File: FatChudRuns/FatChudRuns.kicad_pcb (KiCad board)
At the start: 4 copper layers, 96.9 x 73.9 mm, 104 parts, among them J1 RJ45_Pulse_JXD6-0001NL, J2 Z-21320110021001, J3 FTSH-107-01-L-DV-K-P, J4 TYPE-C-31-M-12, SW1 TS-1187A-B-A-B, SW5 1825360-3, U1 STM32F107RBT6, U2 DP83848I, U3 USBLC6-2SC6, U4 ST730M33R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

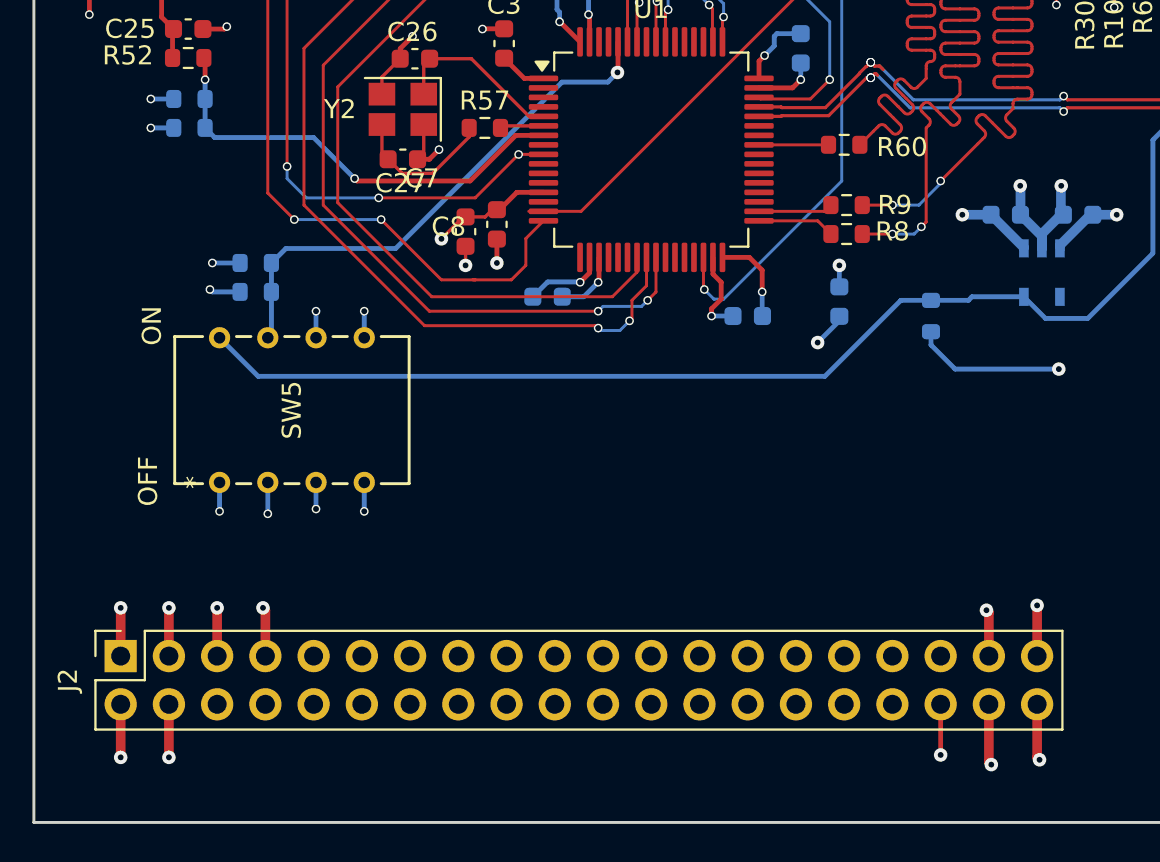
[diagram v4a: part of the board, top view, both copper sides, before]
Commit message: finished initial layout, removed some gpio pins and reorganized them
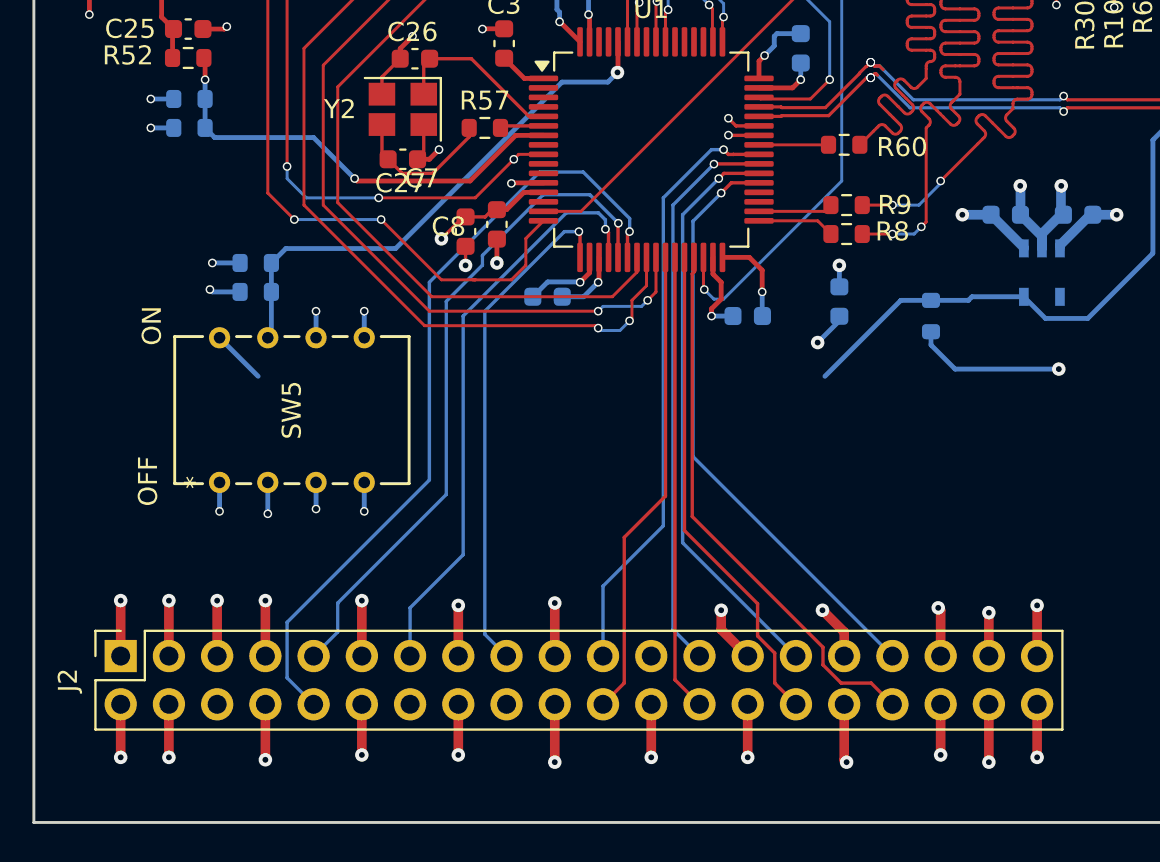
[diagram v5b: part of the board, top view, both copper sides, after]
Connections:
- J2 pad 10: /MCU/PA4 -> /MCU/PA6
- J2 pad 11: /MCU/PC0 -> GND
- J2 pad 12: /MCU/PA5 -> GND
- J2 pad 13: /MCU/PC2 -> /MCU/PA4
- J2 pad 14: /MCU/PA6 -> unconnected-(J2-Pin_14-Pad14)
- J2 pad 15: /MCU/PC3 -> GND
- J2 pad 16: /MCU/PA9 -> GND
- J2 pad 17: /MCU/PC6 -> /MCU/PA3
- J2 pad 18: /MCU/PA10 -> unconnected-(J2-Pin_18-Pad18)
- J2 pad 19: /MCU/PC7 -> GND
- J2 pad 20: /MCU/PB0 -> GND
- J2 pad 21: /MCU/PC8 -> /MCU/PC9
- J2 pad 22: /MCU/PB1 -> /MCU/PB0
- J2 pad 23: /MCU/PC9 -> GND
- J2 pad 24: /MCU/PB2 -> GND
- J2 pad 25: /MCU/PC10 -> /MCU/PC8
- J2 pad 26: /MCU/PB5 -> /MCU/PB1
- J2 pad 27: /MCU/PC11 -> GND
- J2 pad 28: /MCU/PB8 -> GND
- J2 pad 29: /MCU/PC12 -> /MCU/PC7
- J2 pad 30: /MCU/PB9 -> /MCU/PB2
- J2 pad 31: /MCU/PC13 -> GND
- J2 pad 32: /MCU/PB10 -> GND
- J2 pad 33: /MCU/PC14 -> /MCU/PC6
- J2 pad 34: /MCU/PB14 -> /MCU/PB10
- J2 pad 35: /MCU/PC15 -> GND
- J2 pad 36: /MCU/PB15 -> GND
- J2 pad 6: /MCU/PA0 -> +3.3V
- J2 pad 7: +3.3V -> GND
- J2 pad 8: /MCU/PA3 -> GND
- J2 pad 9: /MCU/PD2 -> /MCU/PA5
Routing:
- net GND: track 144.6 -> 188.2 mm, vias 71 -> 87
- net /MCU/PA6: track 0.00 -> 42.0 mm, vias 0 -> 1
- net /MCU/PA5: track 0.00 -> 35.7 mm, vias 0 -> 1
- net /MCU/PC9: track 0.00 -> 31.6 mm, vias 0 -> 1
- net /MCU/PC6: track 0.00 -> 31.6 mm, vias 0 -> 1
- net /MCU/PA4: track 0.00 -> 31.0 mm, vias 0 -> 1
- net /MCU/PC7: track 0.00 -> 30.6 mm, vias 0 -> 1
- net LDO_EN: track 71.4 -> 41.6 mm
- net /MCU/PC8: track 0.00 -> 29.8 mm, vias 0 -> 1
- net /MCU/PB10: track 0.00 -> 28.9 mm
- net /MCU/PA3: track 0.00 -> 26.7 mm, vias 0 -> 1
- net /MCU/PB2: track 0.00 -> 26.0 mm
- net /MCU/PB0: track 0.00 -> 24.9 mm
- net /MCU/PB1: track 0.00 -> 24.1 mm
- net /MCU/PB15: track 2.67 -> 0.00 mm, vias 1 -> 0
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
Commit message: updated constraints, parsed through most drc
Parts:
- moved C26 2.85 mm to (176.5, 128.8), turned to 90 degrees
- moved C3 0.92 mm to (178.1, 126.1)
- moved R46 0.43 mm to (214.6, 110.6)
- moved R57 0.36 mm to (177.3, 131.1)
- moved C27 0.33 mm to (173.6, 132.9)
- moved C6 0.25 mm to (180.8, 140.5)
- moved C22 0.13 mm to (204.9, 135.9)
- moved R31 0.13 mm to (215.2, 113.7)
- moved R34 0.10 mm to (215.2, 111.9)
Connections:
- J2 pad 14: unconnected-(J2-Pin_14-Pad14) -> GND
- J2 pad 18: unconnected-(J2-Pin_18-Pad18) -> GND
- U1 pad 10: /MCU/PC2 -> unconnected-(U1-PC2-Pad10)
- U1 pad 11: /MCU/PC3 -> unconnected-(U1-PC3-Pad11)
- U1 pad 14: /MCU/PA0 -> unconnected-(U1-PA0-Pad14)
- U1 pad 2: /MCU/PC13 -> unconnected-(U1-PC13-Pad2)
- U1 pad 3: /MCU/PC14 -> unconnected-(U1-PC14-Pad3)
- U1 pad 35: /MCU/PB14 -> unconnected-(U1-PB14-Pad35)
- U1 pad 36: /MCU/PB15 -> unconnected-(U1-PB15-Pad36)
- U1 pad 4: /MCU/PC15 -> unconnected-(U1-PC15-Pad4)
- U1 pad 42: /MCU/PA9 -> unconnected-(U1-PA9-Pad42)
- U1 pad 43: /MCU/PA10 -> unconnected-(U1-PA10-Pad43)
- U1 pad 51: /MCU/PC10 -> unconnected-(U1-PC10-Pad51)
- U1 pad 52: /MCU/PC11 -> unconnected-(U1-PC11-Pad52)
- U1 pad 53: /MCU/PC12 -> unconnected-(U1-PC12-Pad53)
- U1 pad 54: /MCU/PD2 -> unconnected-(U1-PD2-Pad54)
- U1 pad 57: /MCU/PB5 -> unconnected-(U1-PB5-Pad57)
- U1 pad 61: /MCU/PB8 -> unconnected-(U1-PB8-Pad61)
- U1 pad 62: /MCU/PB9 -> unconnected-(U1-PB9-Pad62)
- U1 pad 8: /MCU/PC0 -> unconnected-(U1-PC0-Pad8)
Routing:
- net LDO_EN: track 41.6 -> 72.8 mm, vias 0 -> 2
- net Net-(U2-PFBIN1): track 11.6 -> 23.3 mm, vias 2 -> 3
- net /MCU/T_VCP_TX: track 8.72 -> 13.4 mm
- net GND: track 188.2 -> 191.1 mm, vias 87 -> 90
- net /MCU/T_VCP_RX: track 8.76 -> 11.3 mm
- net PWR_DOWN: track 8.12 -> 10.4 mm
- net Net-(J4-D--PadA7): track 5.62 -> 7.45 mm
- net /MCU/PA10: track 1.78 -> 0.00 mm, vias 1 -> 0
- net /MCU/OSC_IN: track 9.25 -> 7.56 mm
- net /MCU/PA9: track 1.62 -> 0.00 mm, vias 1 -> 0
- net Net-(C27-Pad1): track 7.81 -> 8.75 mm
- net USB_D+: track 52.2 -> 51.5 mm, vias 3 -> 2
- net Net-(J4-D+-PadA6): track 5.62 -> 6.25 mm
- net Net-(U2-CRS/CRS_DV/LED_CFG): track 15.8 -> 16.1 mm, vias 1 -> 0
- net USB_D-: track 51.0 -> 50.8 mm, vias 3 -> 2
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
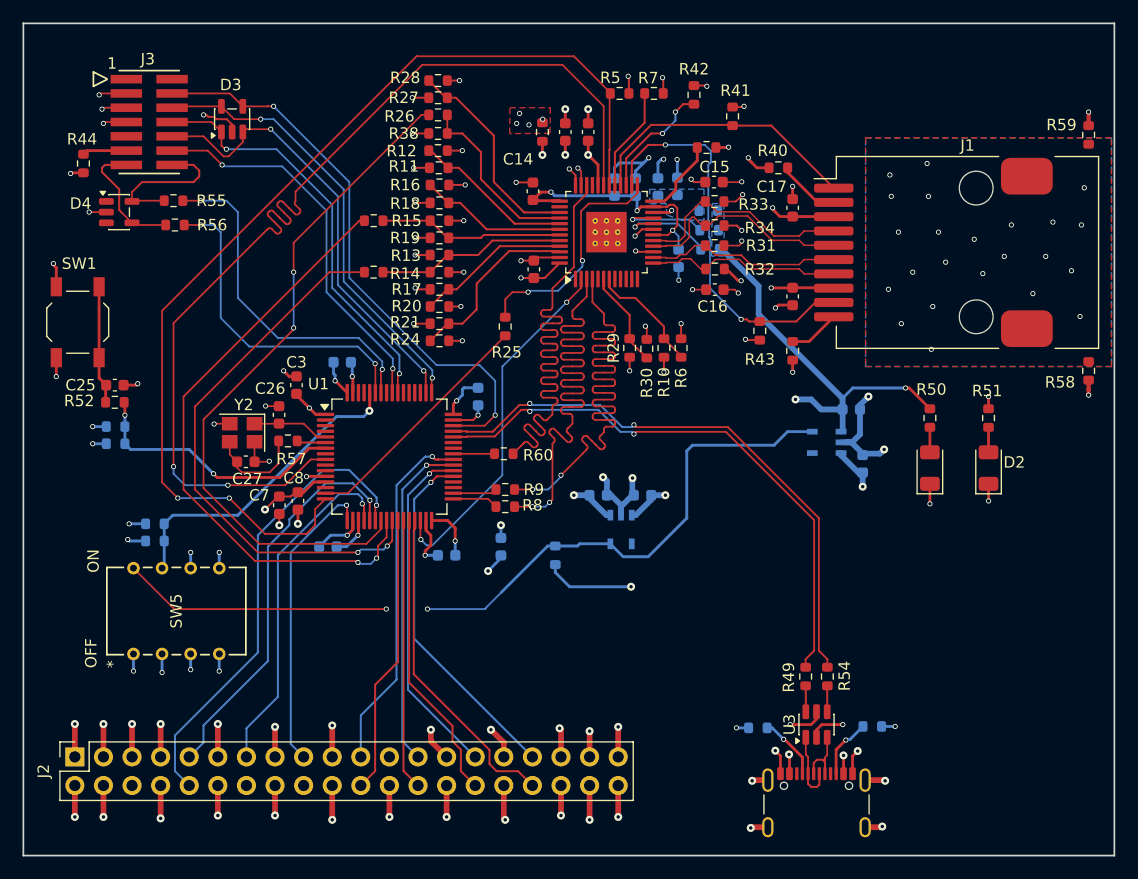
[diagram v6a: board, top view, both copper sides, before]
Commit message: cleared the rest of the drc - layout complete
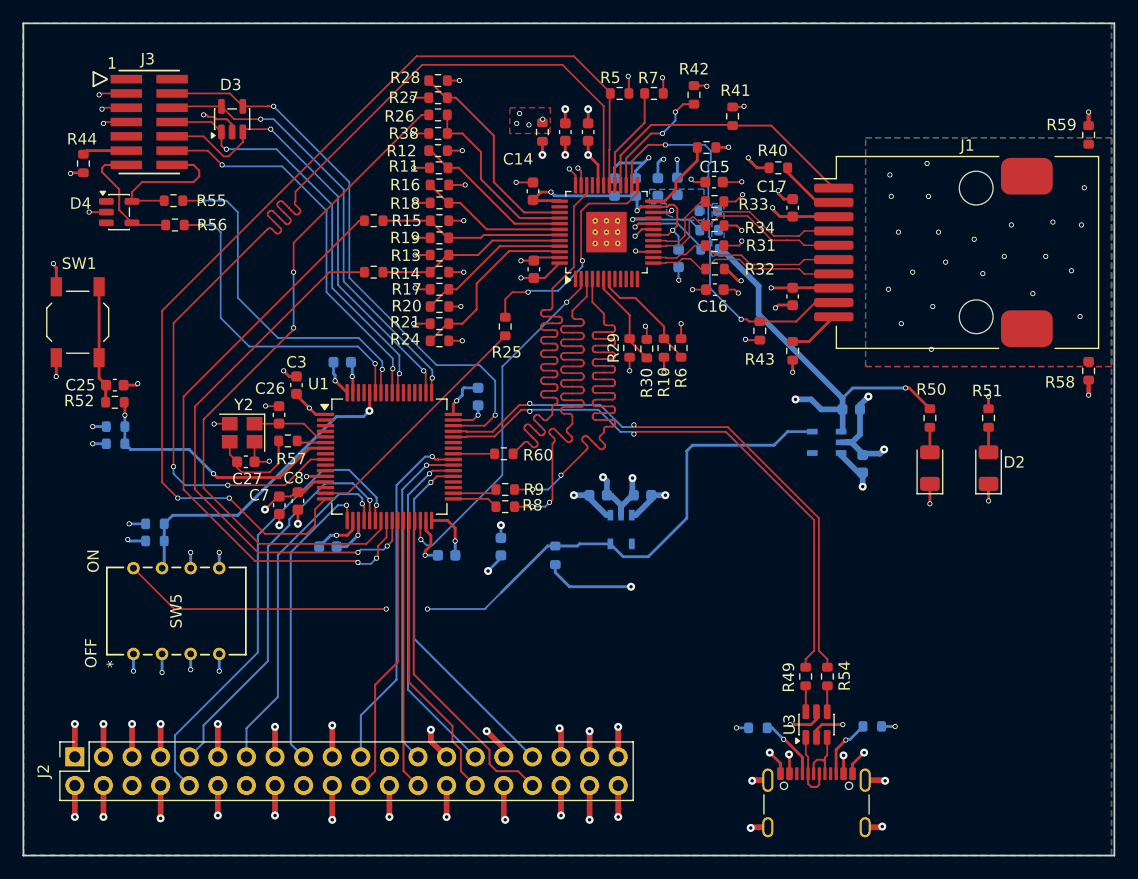
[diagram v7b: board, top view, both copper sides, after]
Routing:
- net GND: track 191.1 -> 191.9 mm
- added copper zone on B.Cu, net GND
- added copper zone on F.Cu, net GND

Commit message: created gerbers, need to fix dfm
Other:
- rule pad_to_mask_clearance: 0.15 -> 0
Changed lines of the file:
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@@
 			(dielectric_constraints yes)
 		)
-		(pad_to_mask_clearance 0.15)
-		(solder_mask_min_width 0.25)
+		(pad_to_mask_clearance 0)
 		(allow_soldermask_bridges_in_footprints yes)
 		(tenting
@@
 		(capping no)
 		(filling no)
-		(zone_defaults)
 		(pcbplotparams
-			(layerselection 0x00000000_00000000_00000000_000000a5)
+			(layerselection 0x00000000_00000000_55555555_5755f5ff)
 			(plot_on_all_layers_selection 0x00000000_00000000_00000000_00000000)
 			(disableapertmacros no)
@@
 			(sketchdnponfab yes)
 			(crossoutdnponfab yes)
-			(subtractmaskfromsilk no)
+			(subtractmaskfromsilk yes)
 			(outputformat 1)
 			(mirror no)
-			(drillshape 1)
+			(drillshape 0)
 			(scaleselection 1)
 			(outputdirectory "")
